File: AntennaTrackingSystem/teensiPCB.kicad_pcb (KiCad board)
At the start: 2 copper layers, 2 parts

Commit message: pcb updates
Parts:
- added REF**: UART1, Connector_PinHeader_2.54mm:PinHeader_1x04_P2.54mm_Vertical, F.Cu at (126.0, 79.0)
- added REF**: I2C ext, Connector_PinHeader_2.54mm:PinHeader_1x04_P2.54mm_Vertical, F.Cu at (161.6, 79.0)
- added REF**: UART2, Connector_PinHeader_2.54mm:PinHeader_1x04_P2.54mm_Vertical, F.Cu at (146.5, 79.0)
- REF**: value XCVR_SAM-M10Q-00B -> SAM-M10Q
- moved REF** 4.70 mm to (134.2, 43.6), turned to 0 degrees
- moved REF** 0.38 mm to (145.0, 63.9)
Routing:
- net (no net): track 0.00 -> 271.9 mm
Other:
- board text added: "GND"
- board text added: "SCL"
- board text added: "SDA"

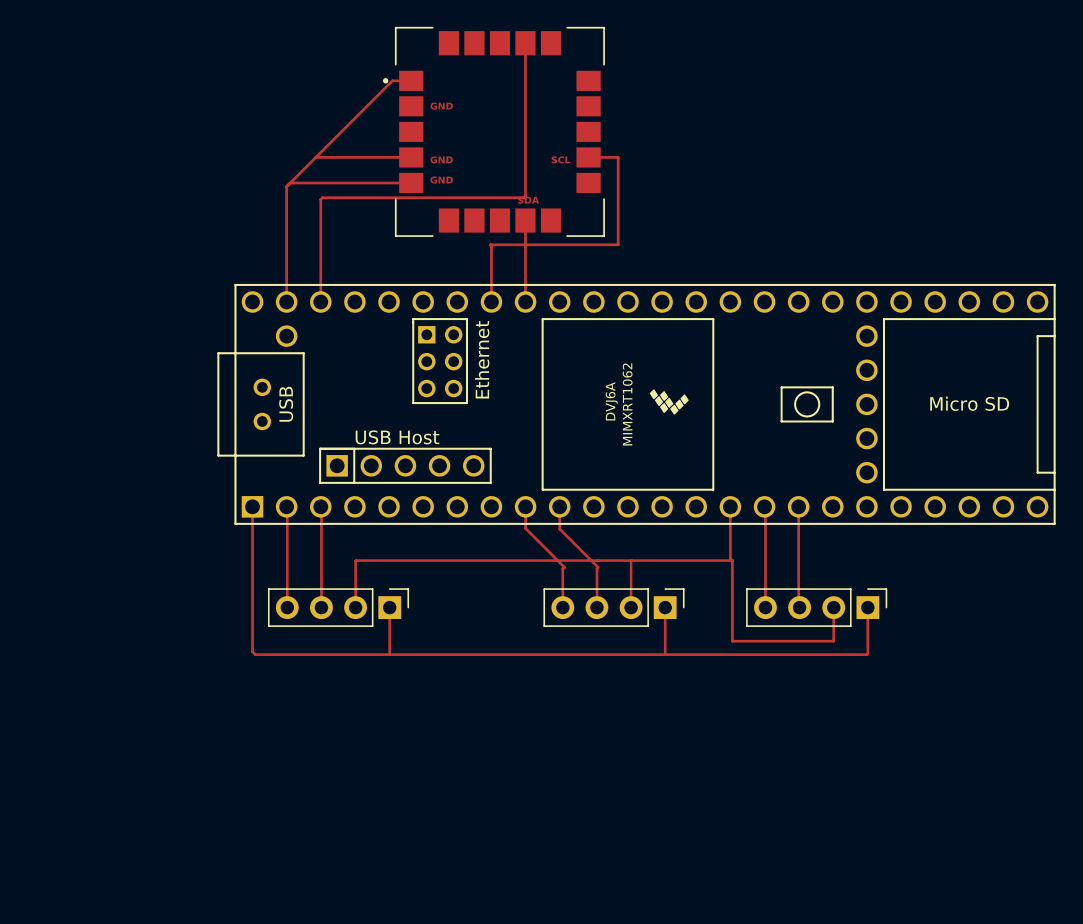
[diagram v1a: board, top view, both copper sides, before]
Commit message: 1st schematic built and added footprints
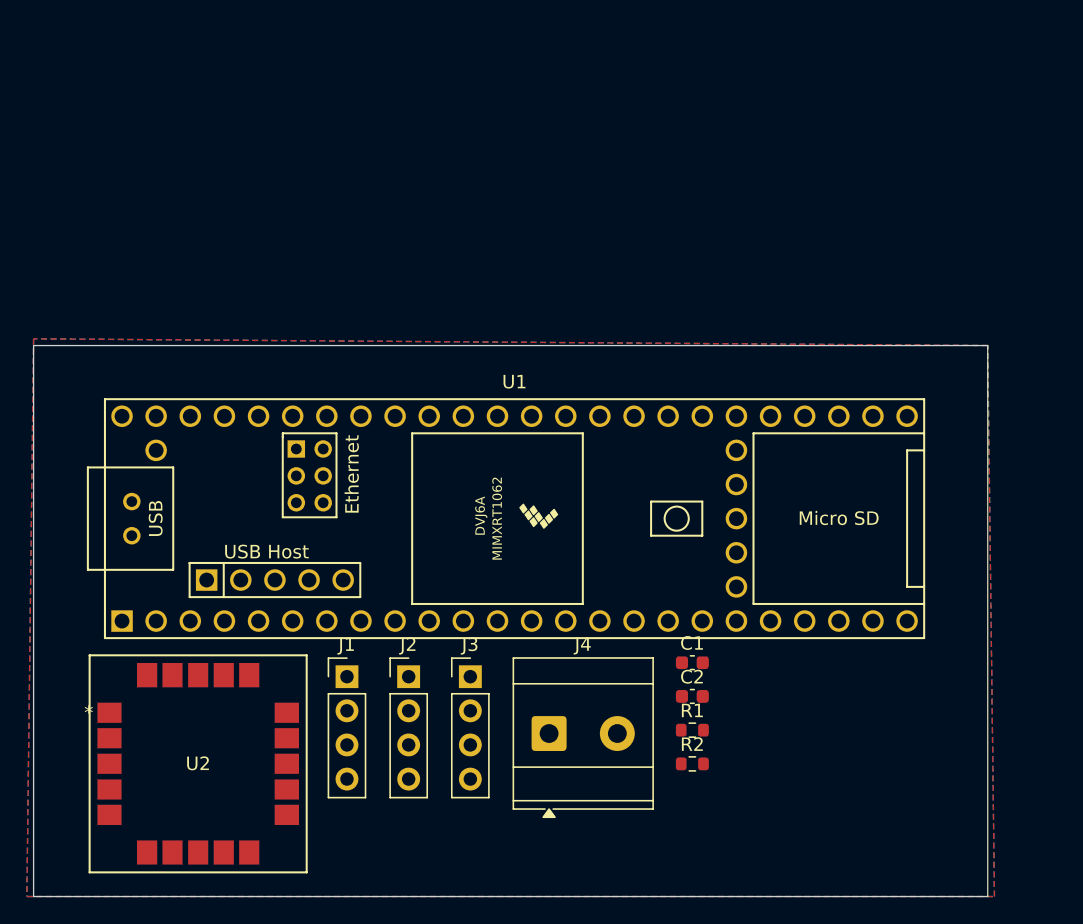
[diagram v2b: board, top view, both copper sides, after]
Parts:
- removed REF**: SAM-M10Q, avionicsKiCadLibrary:XCVR_SAM-M10Q-00B
- removed REF**: Teensy 4.1, avionicsKiCadLibrary:Teensy41
- removed REF**: UART1, Connector_PinHeader_2.54mm:PinHeader_1x04_P2.54mm_Vertical
- removed REF**: I2C ext, Connector_PinHeader_2.54mm:PinHeader_1x04_P2.54mm_Vertical
- removed REF**: UART2, Connector_PinHeader_2.54mm:PinHeader_1x04_P2.54mm_Vertical
- added C1: 0.1uF, Capacitor_SMD:C_0603_1608Metric, F.Cu at (148.5, 83.1)
- added C2: 1uF, Capacitor_SMD:C_0603_1608Metric, F.Cu at (148.5, 85.6)
- added J1: UART1, Connector_PinHeader_2.54mm:PinHeader_1x04_P2.54mm_Vertical, F.Cu at (122.8, 84.1)
- added J2: UART2, Connector_PinHeader_2.54mm:PinHeader_1x04_P2.54mm_Vertical, F.Cu at (127.4, 84.1)
- added J3: I2C ext, Connector_PinHeader_2.54mm:PinHeader_1x04_P2.54mm_Vertical, F.Cu at (132.0, 84.1)
- added J4: screw terminal, TerminalBlock_MetzConnect:TerminalBlock_MetzConnect_Type073_RT02602HBLU_1x02_P5.08mm_Horizontal, F.Cu at (137.9, 88.4)
- added R1: 4.7k, Resistor_SMD:R_0603_1608Metric, F.Cu at (148.5, 88.1)
- added R2: 4.7k, Resistor_SMD:R_0603_1608Metric, F.Cu at (148.5, 90.6)
- added U1: Teensy4.1, Teensy41:Teensy41, F.Cu at (135.3, 72.4)
- added U2: SAM-M10Q-00B, SAM M10Q footprint:SAM-M10Q_UBL, F.Cu at (111.7, 90.6)
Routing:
- net (no net): track 271.9 -> 0.00 mm
- added copper zone on B.Cu, net GND
- added copper zone on F.Cu, net GND
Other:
- board outline added: 71 x 41 mm
- board text removed: "GND"
- board text removed: "SCL"
- board text removed: "SDA"

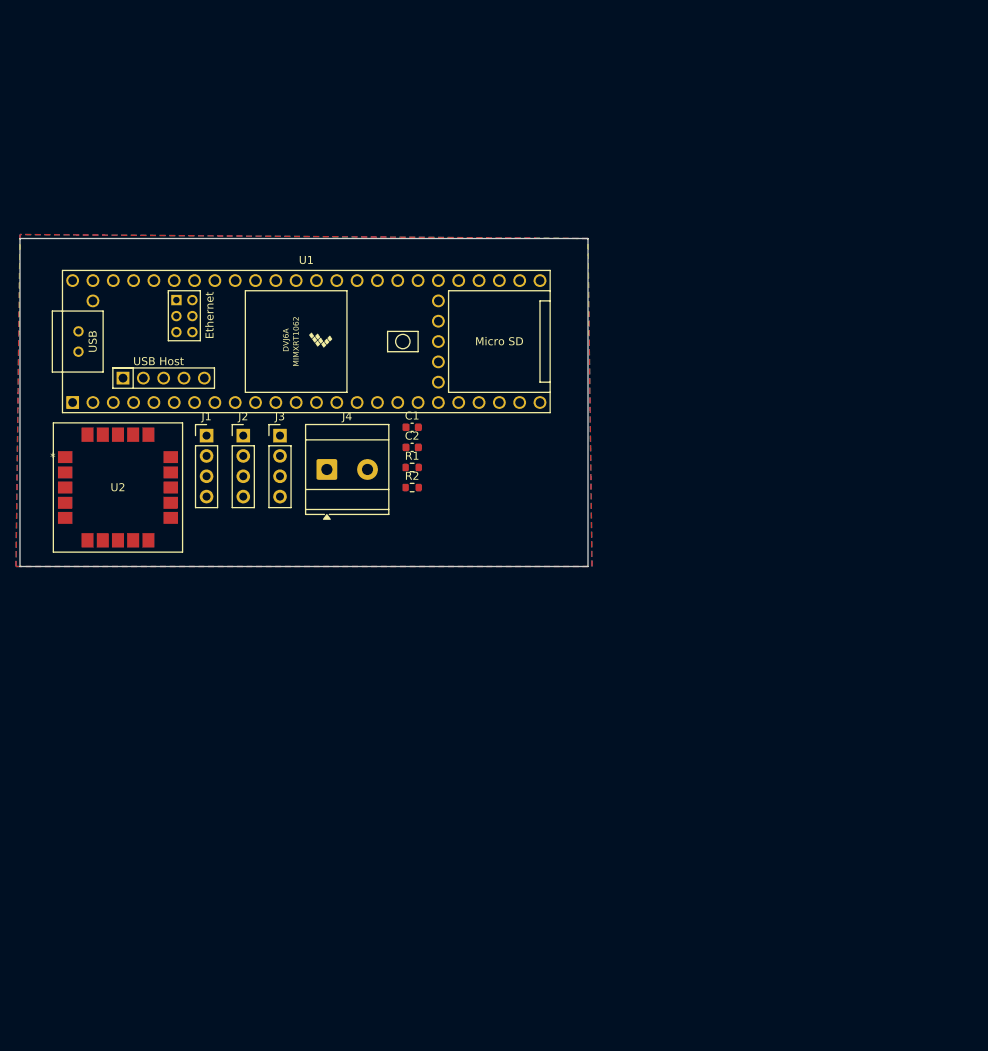
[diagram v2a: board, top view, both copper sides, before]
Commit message: schematic review changes
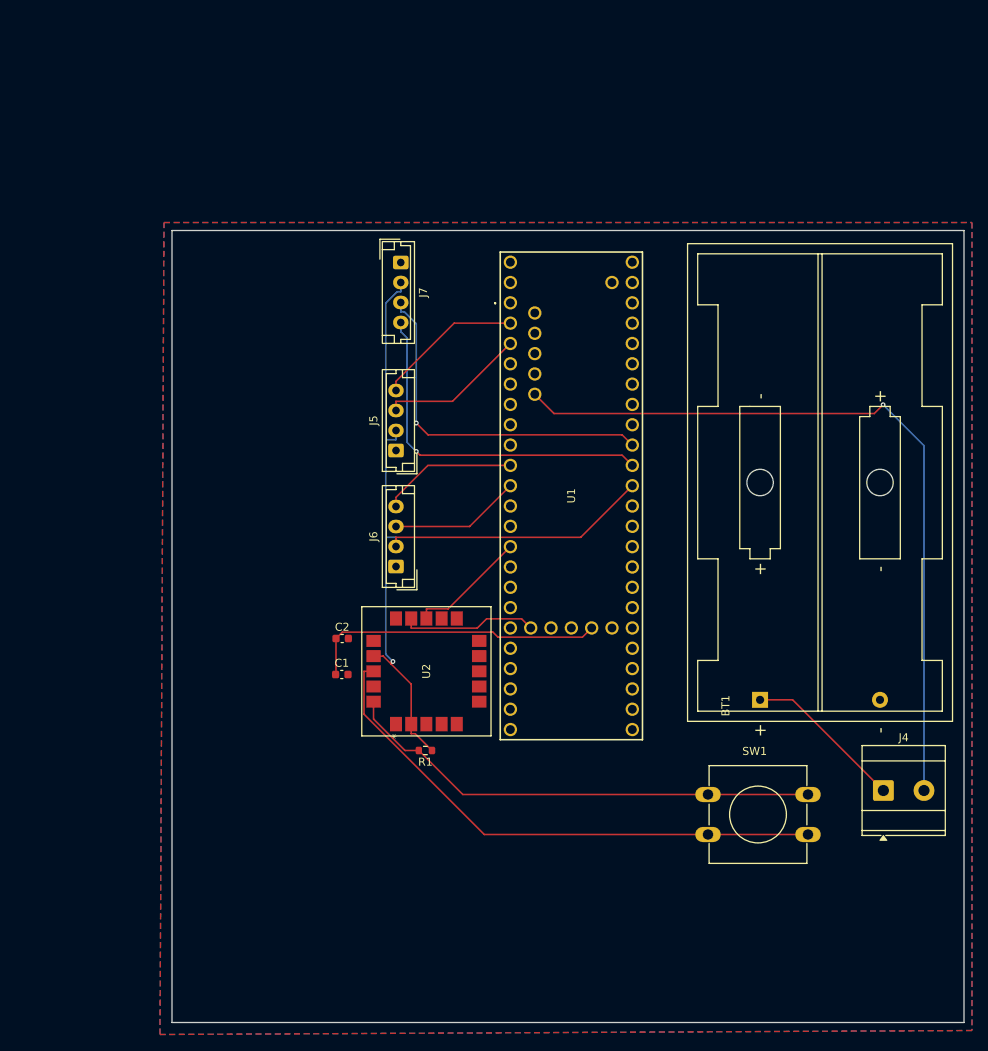
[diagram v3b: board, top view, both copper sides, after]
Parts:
- removed J1: UART1, Connector_PinHeader_2.54mm:PinHeader_1x04_P2.54mm_Vertical
- removed J2: UART2, Connector_PinHeader_2.54mm:PinHeader_1x04_P2.54mm_Vertical
- removed J3: I2C ext, Connector_PinHeader_2.54mm:PinHeader_1x04_P2.54mm_Vertical
- removed R2: 4.7k, Resistor_SMD:R_0603_1608Metric
- added BT1: NiMH Battery (4.8V), Battery:BatteryHolder_Keystone_2462_2xAA, F.Cu at (192.0, 117.2)
- added J5: UART1, Connector_JST:JST_EH_B4B-EH-A_1x04_P2.50mm_Vertical, F.Cu at (146.5, 86.0)
- added J6: UART2, Connector_JST:JST_EH_B4B-EH-A_1x04_P2.50mm_Vertical, F.Cu at (146.5, 100.5)
- added J7: I2C ext, Connector_JST:JST_EH_B4B-EH-A_1x04_P2.50mm_Vertical, F.Cu at (147.1, 62.5)
- added SW1: SW_Push, Button_Switch_THT:SW_PUSH-12mm, F.Cu at (185.5, 129.0)
- U1: footprint Teensy41:Teensy41 -> Teensy41:TEENSY41
- moved J4 80.3 mm to (207.4, 128.5)
- moved U2 44.9 mm to (150.3, 113.6), turned to 90 degrees
- moved R1 35.4 mm to (150.2, 123.5), turned to 180 degrees
- moved C1 32.1 mm to (139.7, 114.0)
- moved U1 26.0 mm to (160.8, 67.5), turned to -90 degrees
- moved C2 25.4 mm to (139.8, 109.5)
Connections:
- C1 pad 1: +3.3V -> Net-(C1-Pad1)
- C2 pad 1: +3.3V -> Net-(C1-Pad1)
- J4 pad 1: GND -> Net-(BT1-+)
- R1 pad 1: +3.3V -> +3V3
- R1 pad 2: Net-(U1-17_A3_TX4_SDA1) -> Net-(R1-Pad2)
- U1 pad 15: +3.3V -> +3V3
- U1 pad 38: Net-(U1-16_A2_RX4_SCL1) -> unconnected-(U1-SCL-Pad38)
- U1 pad 39: Net-(U1-17_A3_TX4_SDA1) -> unconnected-(U1-SDA-Pad39)
- U1 pad 42: unconnected-(U1-20_A6_TX5_LRCLK1-Pad42) -> Net-(U1-TX5)
- U1 pad 43: unconnected-(U1-21_A7_RX5_BCLK1-Pad43) -> Net-(U1-RX5)
- U1 pad 46: +3.3V -> Net-(C1-Pad1)
- U1 pad 49: unconnected-(U1-VUSB-Pad49) -> (no net)
- U1 pad 50: unconnected-(U1-VBAT-Pad50) -> (no net)
- U1 pad 51: unconnected-(U1-3V3-Pad51) -> (no net)
- U1 pad 52: unconnected-(U1-GND-Pad52) -> (no net)
- U1 pad 53: unconnected-(U1-PROGRAM-Pad53) -> (no net)
- U1 pad 55: unconnected-(U1-5V-Pad55) -> (no net)
- U1 pad 57: unconnected-(U1-D+-Pad57) -> (no net)
- U2 pad 12: Net-(U1-16_A2_RX4_SCL1) -> unconnected-(U2-SCL-Pad12)
- U2 pad 13: unconnected-(U2-TXD-Pad13) -> Net-(U1-TX5)
- U2 pad 14: unconnected-(U2-RXD-Pad14) -> Net-(U1-RX5)
- U2 pad 17: +3.3V -> +3V3
- U2 pad 18: unconnected-(U2-RESET_N-Pad18) -> Net-(U2-RESET_N)
- U2 pad 2: unconnected-(U2-V_IO-Pad2) -> +3V3
- U2 pad 20: GND -> Net-(R1-Pad2)
- U2 pad 9: Net-(U1-17_A3_TX4_SDA1) -> unconnected-(U2-SDA-Pad9)
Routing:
- net +3V3: track 0.00 -> 103.2 mm, vias 0 -> 1
- net Net-(J4-Pin_2): track 0.00 -> 95.3 mm, vias 0 -> 1
- net Net-(U2-RESET_N): track 0.00 -> 68.3 mm
- net Net-(R1-Pad2): track 0.00 -> 60.4 mm
- net Net-(J7-Pin_4): track 0.00 -> 44.6 mm, vias 0 -> 1
- net Net-(J7-Pin_3): track 0.00 -> 44.3 mm, vias 0 -> 1
- net Net-(C1-Pad1): track 0.00 -> 37.5 mm
- net Net-(BT1-+): track 0.00 -> 20.1 mm
- net Net-(J5-Pin_4): track 0.00 -> 18.5 mm
- net Net-(J5-Pin_3): track 0.00 -> 18.4 mm
- net Net-(J6-Pin_4): track 0.00 -> 17.1 mm
- net Net-(U1-RX5): track 0.00 -> 17.1 mm
- net Net-(J6-Pin_3): track 0.00 -> 16.4 mm
- net Net-(U1-TX5): track 0.00 -> 14.9 mm
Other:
- board size 71 x 41 mm -> 99 x 99 mm

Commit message: correct connector footprint
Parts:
- J5, J6, J7: footprint Connector_JST:JST_EH_B4B-EH-A_1x04_P2.50mm_Vertical -> Connector_JST:JST_XH_B4B-XH-A_1x04_P2.50mm_Vertical

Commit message: back to I2C and other small updates
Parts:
- removed BT1: NiMH Battery (4.8V), Battery:BatteryHolder_Keystone_2462_2xAA
- removed J4: screw terminal, TerminalBlock_MetzConnect:TerminalBlock_MetzConnect_Type073_RT02602HBLU_1x02_P5.08mm_Horizontal
- added J1: screw terminal, Connector_JST:JST_XH_B2B-XH-A_1x02_P2.50mm_Vertical, F.Cu at (209.0, 128.5)
- added R2: R, Resistor_SMD:R_0603_1608Metric, F.Cu at (182.7, 129.0)
- added R3: R, Resistor_SMD:R_0603_1608Metric, F.Cu at (182.7, 133.5)
- moved J7 37.0 mm to (183.0, 71.5), turned to 90 degrees
- moved C1 36.5 mm to (176.2, 114.0)
- moved C2 36.5 mm to (176.2, 109.5)
- moved J5 36.5 mm to (183.0, 86.0)
- moved J6 36.5 mm to (183.0, 100.5)
- moved U1 36.5 mm to (197.3, 67.5)
- moved U2 36.5 mm to (186.8, 113.6)
- moved R1 32.5 mm to (182.7, 125.0)
- moved SW1 2.50 mm to (188.0, 129.0)
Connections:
- J5 pad 2: +3V3 -> Net-(J5-Pin_2)
- J5 pad 4: Net-(J5-Pin_4) -> +3V3
- J6 pad 2: +3V3 -> Net-(J6-Pin_2)
- J6 pad 4: Net-(J6-Pin_4) -> +3V3
- J7 pad 2: +3V3 -> Net-(J7-Pin_2)
- J7 pad 4: Net-(J7-Pin_4) -> +3V3
- R1 pad 2: Net-(R1-Pad2) -> Net-(U2-RESET_N)
- SW1 pad 1: Net-(R1-Pad2) -> GND
- U1 pad 16: Net-(J7-Pin_4) -> Net-(J7-Pin_2)
- U1 pad 2: Net-(J5-Pin_4) -> Net-(J5-Pin_2)
- U1 pad 38: unconnected-(U1-SCL-Pad38) -> Net-(U1-SCL)
- U1 pad 39: unconnected-(U1-SDA-Pad39) -> Net-(U1-SDA)
- U1 pad 42: Net-(U1-TX5) -> unconnected-(U1-TX5-Pad42)
- U1 pad 43: Net-(U1-RX5) -> unconnected-(U1-RX5-Pad43)
- U1 pad 47: GND -> Net-(J1-Pin_2)
- U1 pad 48: Net-(J4-Pin_2) -> /+V
- U1 pad 9: Net-(J6-Pin_4) -> Net-(J6-Pin_2)
- U2 pad 12: unconnected-(U2-SCL-Pad12) -> Net-(U1-SCL)
- U2 pad 13: Net-(U1-TX5) -> unconnected-(U2-TXD-Pad13)
- U2 pad 14: Net-(U1-RX5) -> unconnected-(U2-RXD-Pad14)
- U2 pad 20: Net-(R1-Pad2) -> GND
- U2 pad 9: unconnected-(U2-SDA-Pad9) -> Net-(U1-SDA)
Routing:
- net +3V3: track 103.2 -> 0.00 mm, vias 1 -> 0
- net Net-(J4-Pin_2): track 95.3 -> 0.00 mm, vias 1 -> 0
- net Net-(U2-RESET_N): track 68.3 -> 0.00 mm
- net Net-(R1-Pad2): track 60.4 -> 0.00 mm
- net Net-(J7-Pin_4): track 44.6 -> 0.00 mm, vias 1 -> 0
- net Net-(J7-Pin_3): track 44.3 -> 0.00 mm, vias 1 -> 0
- net Net-(C1-Pad1): track 37.5 -> 0.00 mm
- net Net-(BT1-+): track 20.1 -> 0.00 mm
- net Net-(J5-Pin_4): track 18.5 -> 0.00 mm
- net Net-(J5-Pin_3): track 18.4 -> 0.00 mm
- net Net-(J6-Pin_4): track 17.1 -> 0.00 mm
- net Net-(U1-RX5): track 17.1 -> 0.00 mm
- net Net-(J6-Pin_3): track 16.4 -> 0.00 mm
- net Net-(U1-TX5): track 14.9 -> 0.00 mm

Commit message: final changes
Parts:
- R2, R3: value R -> 4.7k
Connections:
- U2 pad 3: unconnected-(U2-V_BCKP-Pad3) -> +3V3
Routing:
- net +3V3: track 0.00 -> 115.9 mm, vias 0 -> 1
- net Net-(U1-SDA): track 0.00 -> 56.1 mm, vias 0 -> 2
- net Net-(U1-SCL): track 0.00 -> 55.3 mm, vias 0 -> 2
- net /+V: track 0.00 -> 53.1 mm
- net Net-(U2-RESET_N): track 0.00 -> 48.6 mm
- net Net-(J7-Pin_2): track 0.00 -> 46.8 mm, vias 0 -> 1
- net Net-(J7-Pin_3): track 0.00 -> 46.1 mm, vias 0 -> 1
- net Net-(C1-Pad1): track 0.00 -> 37.5 mm
- net Net-(J6-Pin_2): track 0.00 -> 23.8 mm
- net Net-(J5-Pin_2): track 0.00 -> 23.7 mm
- net Net-(J1-Pin_2): track 0.00 -> 21.6 mm
- net Net-(J5-Pin_3): track 0.00 -> 17.8 mm
- net Net-(J6-Pin_3): track 0.00 -> 16.4 mm
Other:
- board size 99 x 99 mm -> 45 x 84 mm

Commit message: forgot tracks
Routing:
- net Net-(U1-SCL): track 55.3 -> 66.6 mm
- net Net-(U2-RESET_N): track 48.6 -> 41.7 mm
- net Net-(J7-Pin_3): track 46.1 -> 39.4 mm, vias 1 -> 0
- net +3V3: track 115.9 -> 112.1 mm, vias 1 -> 0
- net Net-(U1-SDA): track 56.1 -> 52.9 mm, vias 2 -> 1
- net Net-(J7-Pin_2): track 46.8 -> 48.1 mm, vias 1 -> 0
- net Net-(J5-Pin_2): track 23.7 -> 24.0 mm, vias 0 -> 1
- net Net-(C1-Pad1): track 37.5 -> 37.4 mm, vias 0 -> 1
